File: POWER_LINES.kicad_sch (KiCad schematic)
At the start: 30 parts

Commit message: 2nd ADE
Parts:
- added H5: 0031.8201.G, 00318201G, symbol SamacSys_Parts:0031.8201.G
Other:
- note added: "Connector and fuse"
- moved on the sheet: C39, C40, C41, C42, C43, C44, C45, C46, Csns1, Csns2, R26, R27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

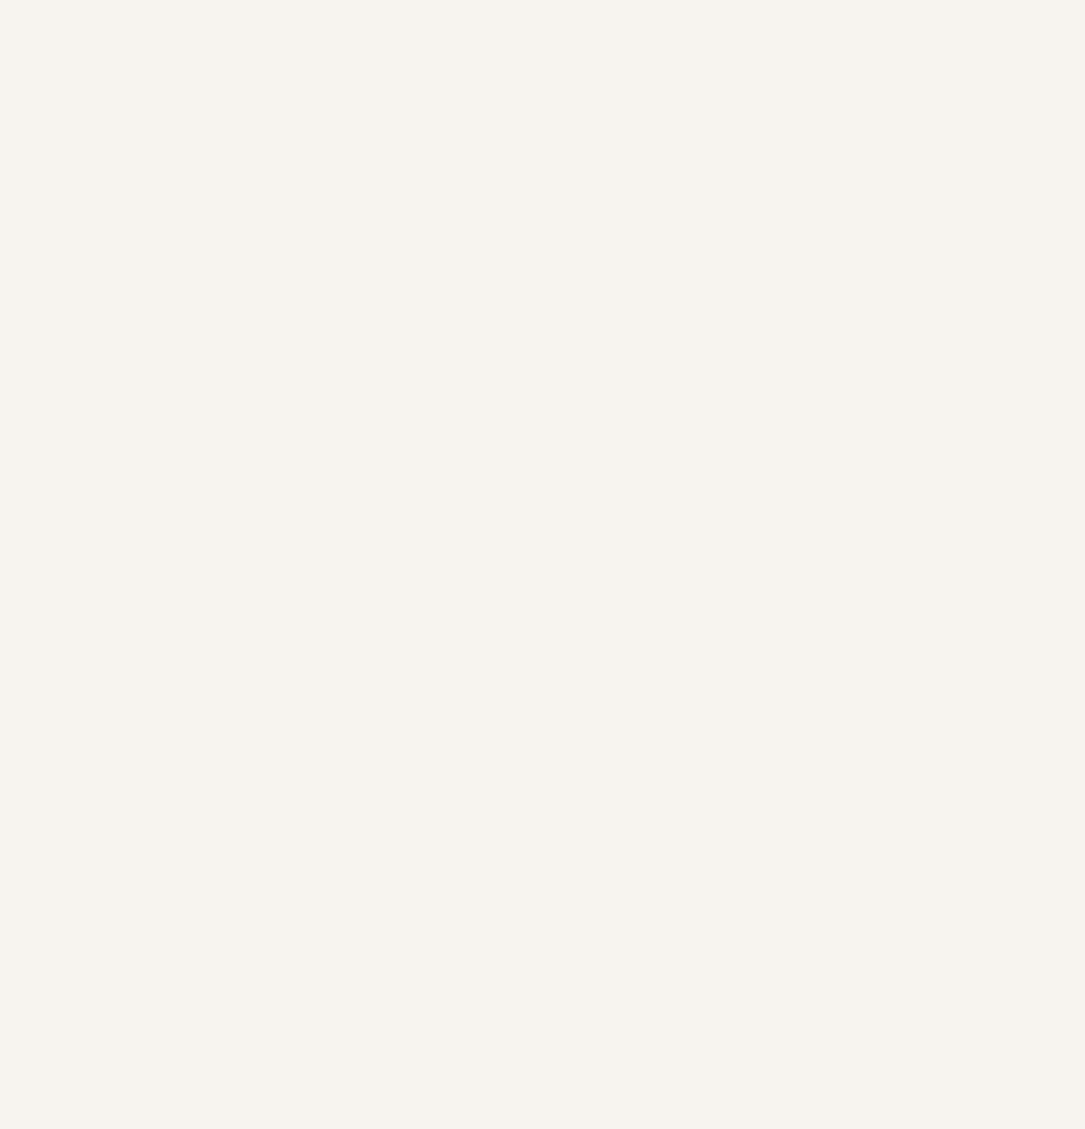
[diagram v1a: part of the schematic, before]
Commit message: ADDED RELAY
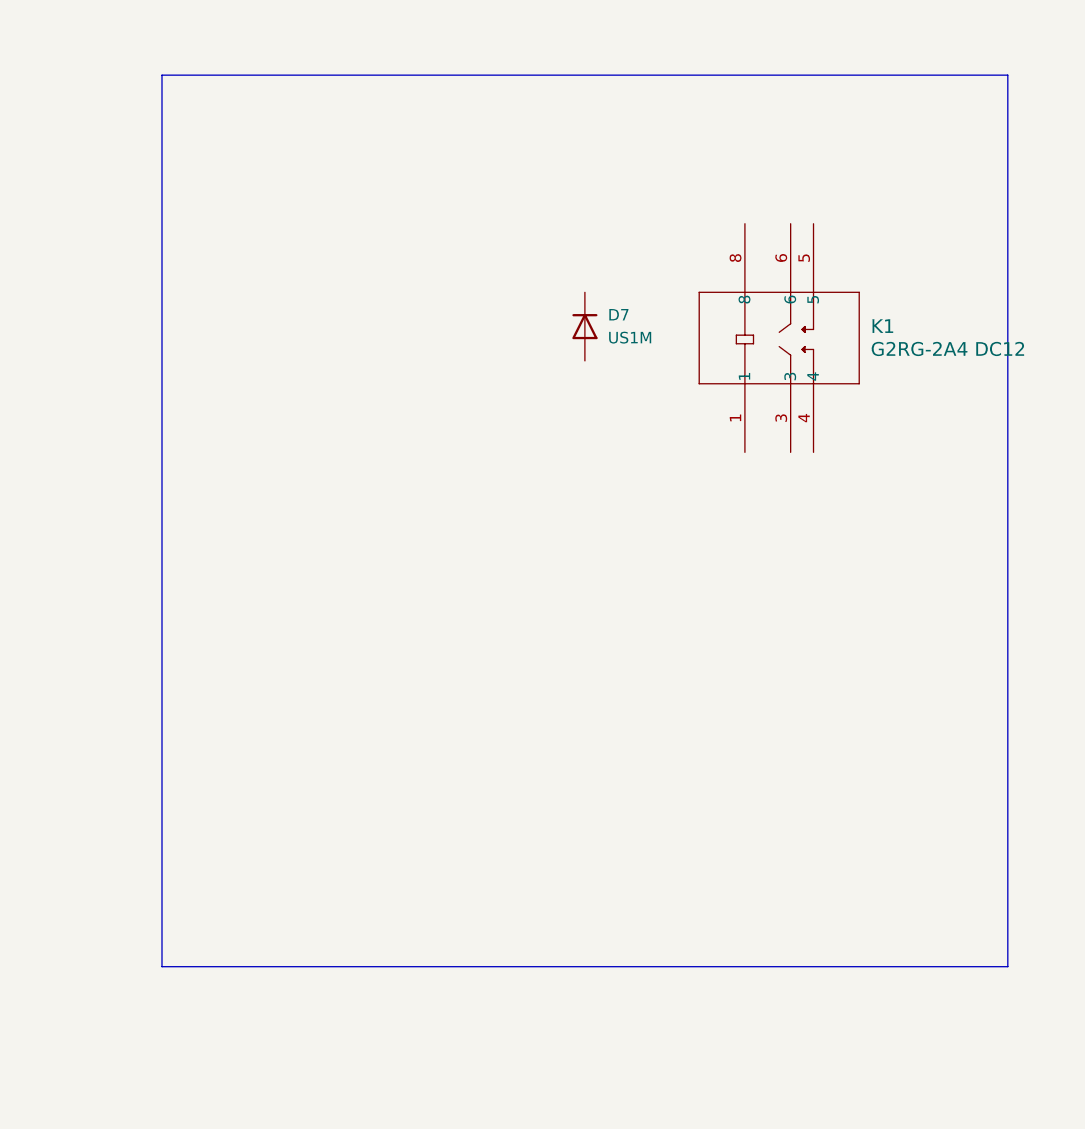
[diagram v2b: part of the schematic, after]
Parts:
- added D7: US1M, Diode_SMD:D_SMA, symbol Diode:US1M
- added K1: G2RG-2A4 DC12, RELAY_G2R-2A AC12_OMR, symbol SmartSupplyLib:G2RG-2A4_DC12
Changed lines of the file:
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@@
 	)
 	(rectangle
+		(start 175.26 20.32)
+		(end 269.24 119.38)
+		(stroke
+			(width 0)
+			(type default)
+		)
+		(fill
+			(type none)
+		)
+	)
+	(rectangle
 		(start 13.97 96.52)
 		(end 83.82 146.05)
@@
 	)
 	(symbol
+		(lib_id "SmartSupplyLib:G2RG-2A4_DC12")
+		(at 241.3 78.74 90)
+		(unit 1)
+		(body_style 1)
+		(exclude_from_sim no)
+		(in_bom yes)
+		(on_board yes)
+		(in_pos_files yes)
+		(dnp no)
+		(fields_autoplaced yes)
+		(property "Reference" "K1"
+			(at 254 48.2599 90)
+			(show_name no)
+			(do_not_autoplace no)
+			(effects
+				(font
+					(size 1.524 1.524)
+				)
+				(justify right)
+			)
+		)
+		(property "Value" "G2RG-2A4 DC12"
+			(at 254 50.7999 90)
+			(show_name no)
+			(do_not_autoplace no)
+			(effects
+				(font
+					(size 1.524 1.524)
+				)
+				(justify right)
+			)
+		)
+		(property "Footprint" "RELAY_G2R-2A AC12_OMR"
+			(at 240.03 62.23 0)
+			(hide yes)
+			(show_name no)
+			(do_not_autoplace no)
+			(effects
+				(font
+					(size 1.27 1.27)
+					(italic yes)
+				)
+			)
+		)
+		(property "Datasheet" "G2RG-2A4 DC12"
+			(at 240.03 62.23 0)
+			(hide yes)
+			(show_name no)
+			(do_not_autoplace no)
+			(effects
+				(font
+					(size 1.27 1.27)
+					(italic yes)
+				)
+			)
+		)
+		(property "Description" ""
+			(at 241.3 78.74 0)
+			(hide yes)
+			(show_name no)
+			(do_not_autoplace no)
+			(effects
+				(font
+					(size 1.27 1.27)
+				)
+			)
+		)
+		(pin "5"
+		)
+		(pin "1"
+		)
+		(pin "8"
+		)
+		(pin "3"
+		)
+		(pin "4"
+		)
+		(pin "6"
+		)
+		(instances
+			(project "smart_supply"
+				(path "/487ef637-7a03-4925-80c1-798e0c6f0bbd/34ab41b0-567d-4411-99e8-070d64ace837"
+					(reference "K1")
+					(unit 1)
+				)
+			)
+		)
+	)
+	(symbol
 		(lib_id "Device:R")
 		(at 24.13 107.95 90)
@@
 					(unit 1)
 				)
+			)
+		)
+	)
+	(symbol
+		(lib_id "Diode:US1M")
+		(at 222.25 48.26 270)
+		(unit 1)
+		(body_style 1)
+		(exclude_from_sim no)
+		(in_bom yes)
+		(on_board yes)
+		(in_pos_files yes)
+		(dnp no)
+		(fields_autoplaced yes)
+		(property "Reference" "D7"
+			(at 224.79 46.9899 90)
+			(show_name no)
+			(do_not_autoplace no)
+			(effects
+				(font
+					(size 1.27 1.27)
+				)
+				(justify left)
+			)
+		)
+		(property "Value" "US1M"
+			(at 224.79 49.5299 90)
+			(show_name no)
+			(do_not_autoplace no)
+			(effects
+				(font
+					(size 1.27 1.27)
+				)
+				(justify left)
+			)
+		)
+		(property "Footprint" "Diode_SMD:D_SMA"
+			(at 217.805 48.26 0)
+			(hide yes)
+			(show_name no)
+			(do_not_autoplace no)
+			(effects
+				(font
+					(size 1.27 1.27)
+				)
+			)
+		)
+		(property "Datasheet" "https://www.diodes.com/assets/Datasheets/ds16008.pdf"
+			(at 222.25 48.26 0)
+			(hide yes)
+			(show_name no)
+			(do_not_autoplace no)
+			(effects
+				(font
+					(size 1.27 1.27)
+				)
+			)
+		)
+		(property "Description" "1000V, 1A, General Purpose Rectifier Diode, SMA(DO-214AC)"
+			(at 222.25 48.26 0)
+			(hide yes)
+			(show_name no)
+			(do_not_autoplace no)
+			(effects
+				(font
+					(size 1.27 1.27)
+				)
+			)
+		)
+		(property "Sim.Device" "D"
+			(at 222.25 48.26 0)
+			(hide yes)
+			(show_name no)
+			(do_not_autoplace no)
+			(effects
+				(font
+					(size 1.27 1.27)
+				)
+			)
+		)
+		(property "Sim.Pins" "1=K 2=A"
+			(at 222.25 48.26 0)
+			(hide yes)
+			(show_name no)
+			(do_not_autoplace no)
+			(effects
+				(font
+					(size 1.27 1.27)
+				)
+			)
+		)
+		(pin "1"
+		)
+		(pin "2"
+		)
+		(instances
+			(project "smart_supply"
+				(path "/487ef637-7a03-4925-80c1-798e0c6f0bbd/34ab41b0-567d-4411-99e8-070d64ace837"
+					(reference "D7")
+					(unit 1)
+				)

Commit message: relay connections
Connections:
- net at K1.1: now also D7.2 (A)
- net +5V: now reaches K1.8
- net +5V: now also D7.1 (K)
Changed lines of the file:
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@@
+	)
+	(junction
+		(at 222.25 34.29)
+		(diameter 0)
+		(color 0 0 0 0)
 	)
 	(junction
@@
 	(wire
 		(pts
+			(xy 222.25 34.29) (xy 240.03 34.29)
+		)
+		(stroke
+			(width 0)
+			(type default)
+		)
+	)
+	(wire
+		(pts
 			(xy 49.53 17.78) (xy 55.88 17.78)
 		)
@@
 	(wire
 		(pts
+			(xy 222.25 52.07) (xy 222.25 64.77)
+		)
+		(stroke
+			(width 0)
+			(type default)
+		)
+	)
+	(wire
+		(pts
 			(xy 73.66 114.3) (xy 73.66 116.84)
 		)
@@
 	(wire
 		(pts
+			(xy 240.03 34.29) (xy 240.03 36.83)
+		)
+		(stroke
+			(width 0)
+			(type default)
+		)
+	)
+	(wire
+		(pts
 			(xy 52.07 184.15) (xy 52.07 187.96)
 		)
@@
 	(wire
 		(pts
+			(xy 222.25 27.94) (xy 222.25 34.29)
+		)
+		(stroke
+			(width 0)
+			(type default)
+		)
+	)
+	(wire
+		(pts
 			(xy 53.34 154.94) (xy 57.15 154.94)
 		)
@@
 	(wire
 		(pts
+			(xy 240.03 62.23) (xy 240.03 64.77)
+		)
+		(stroke
+			(width 0)
+			(type default)
+		)
+	)
+	(wire
+		(pts
 			(xy 97.79 124.46) (xy 97.79 135.89)
 		)
@@
 	(wire
 		(pts
+			(xy 222.25 34.29) (xy 222.25 44.45)
+		)
+		(stroke
+			(width 0)
+			(type default)
+		)
+	)
+	(wire
+		(pts
 			(xy 127 125.73) (xy 127 123.19)
 		)
@@
 		(pts
 			(xy 127 186.69) (xy 130.81 186.69)
+		)
+		(stroke
+			(width 0)
+			(type default)
+		)
+	)
+	(wire
+		(pts
+			(xy 222.25 64.77) (xy 240.03 64.77)
 		)
 		(stroke
@@
 					(unit 1)
 				)
+			)
+		)
+	)
+	(symbol
+		(lib_id "power:+3.3V")
+		(at 222.25 27.94 0)
+		(unit 1)
+		(body_style 1)
+		(exclude_from_sim no)
+		(in_bom yes)
+		(on_board yes)
+		(in_pos_files yes)
+		(dnp no)
+		(fields_autoplaced yes)
+		(property "Reference" "#PWR033"
+			(at 222.25 31.75 0)
+			(hide yes)
+			(show_name no)
+			(do_not_autoplace no)
+			(effects
+				(font
+					(size 1.27 1.27)
+				)
+			)
+		)
+		(property "Value" "+5V"
+			(at 222.25 22.86 0)
+			(show_name no)
+			(do_not_autoplace no)
+			(effects
+				(font
+					(size 1.27 1.27)
+				)
+			)
+		)
+		(property "Footprint" "Package_DFN_QFN:Diodes_UDFN3810-9_TYPE_B"
+			(at 222.25 27.94 0)
+			(hide yes)
+			(show_name no)
+			(do_not_autoplace no)
+			(effects
+				(font
+					(size 1.27 1.27)
+				)
+			)
+		)
+		(property "Datasheet" ""
+			(at 222.25 27.94 0)
+			(hide yes)
+			(show_name no)
+			(do_not_autoplace no)
+			(effects
+				(font
+					(size 1.27 1.27)
+				)
+			)
+		)
+		(property "Description" "Power symbol creates a global label with name \"+3.3V\""
+			(at 222.25 27.94 0)
+			(hide yes)
+			(show_name no)
+			(do_not_autoplace no)
+			(effects
+				(font
+					(size 1.27 1.27)
+				)
+			)
+		)
+		(pin "1"
+		)
+		(instances
+			(project "smart_supply"
+				(path "/487ef637-7a03-4925-80c1-798e0c6f0bbd/34ab41b0-567d-4411-99e8-070d64ace837"
+					(reference "#PWR033")
+					(unit 1)
+				)

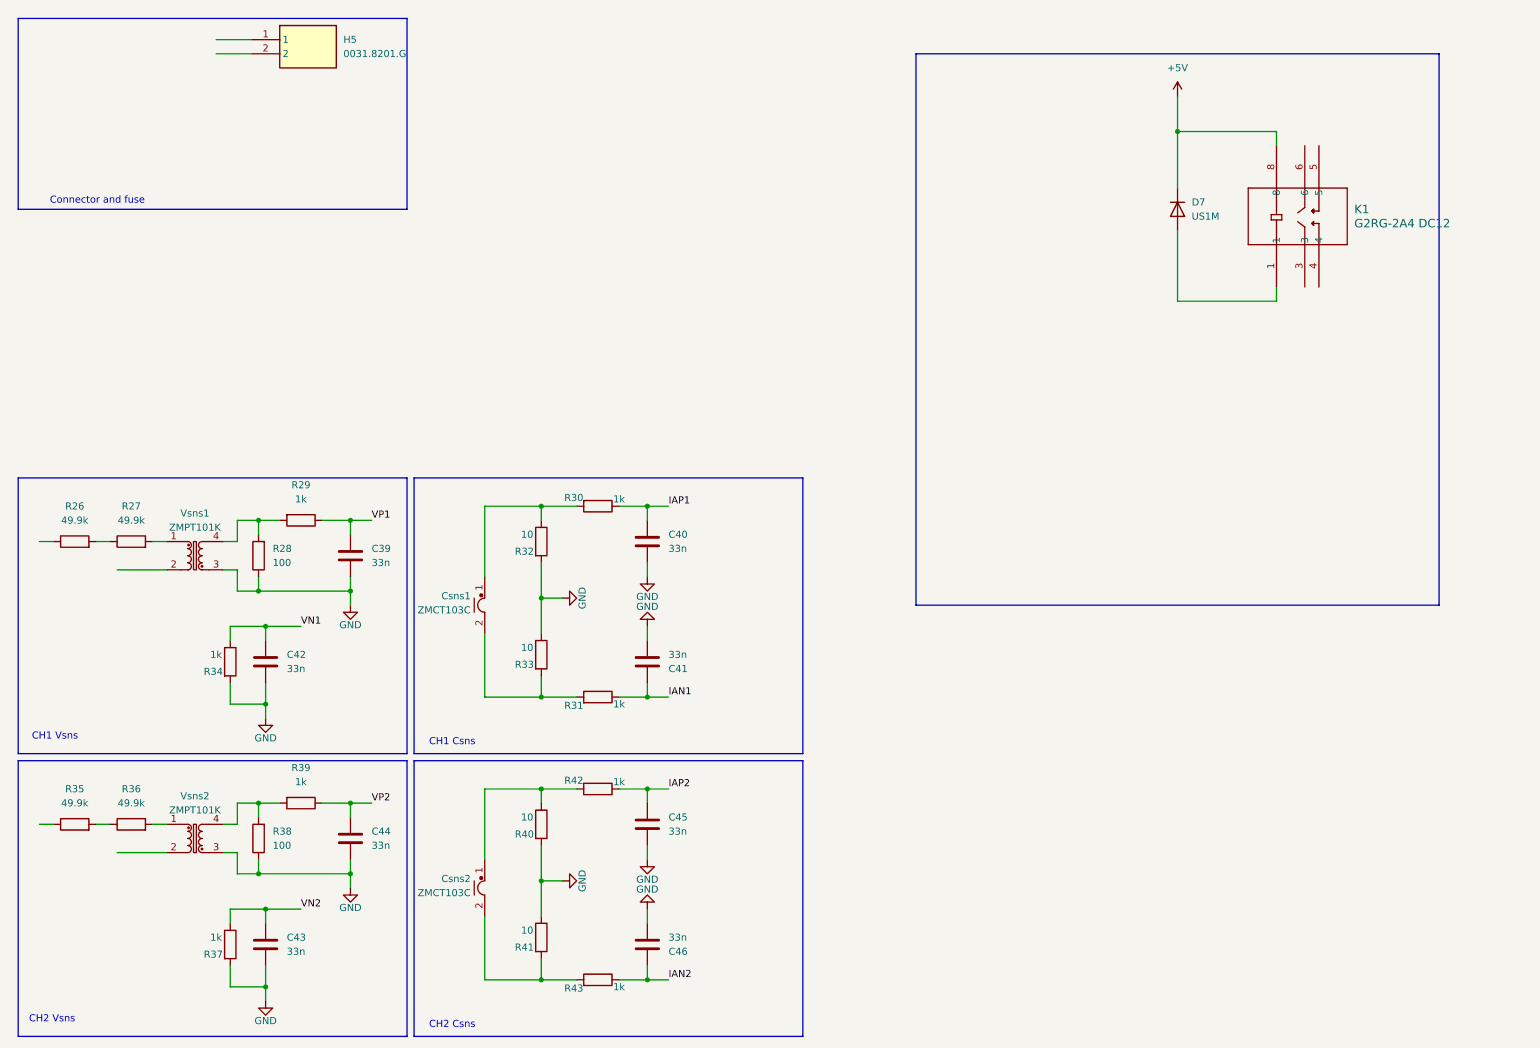
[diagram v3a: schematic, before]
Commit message: POWER LINE SHEET DRAFT FINISHED
Added CH2 transformer, fuses and connectors. Foorprints TBD. Relay modules finished and assigned to MCU. VSNS and CSNS connected to lines.
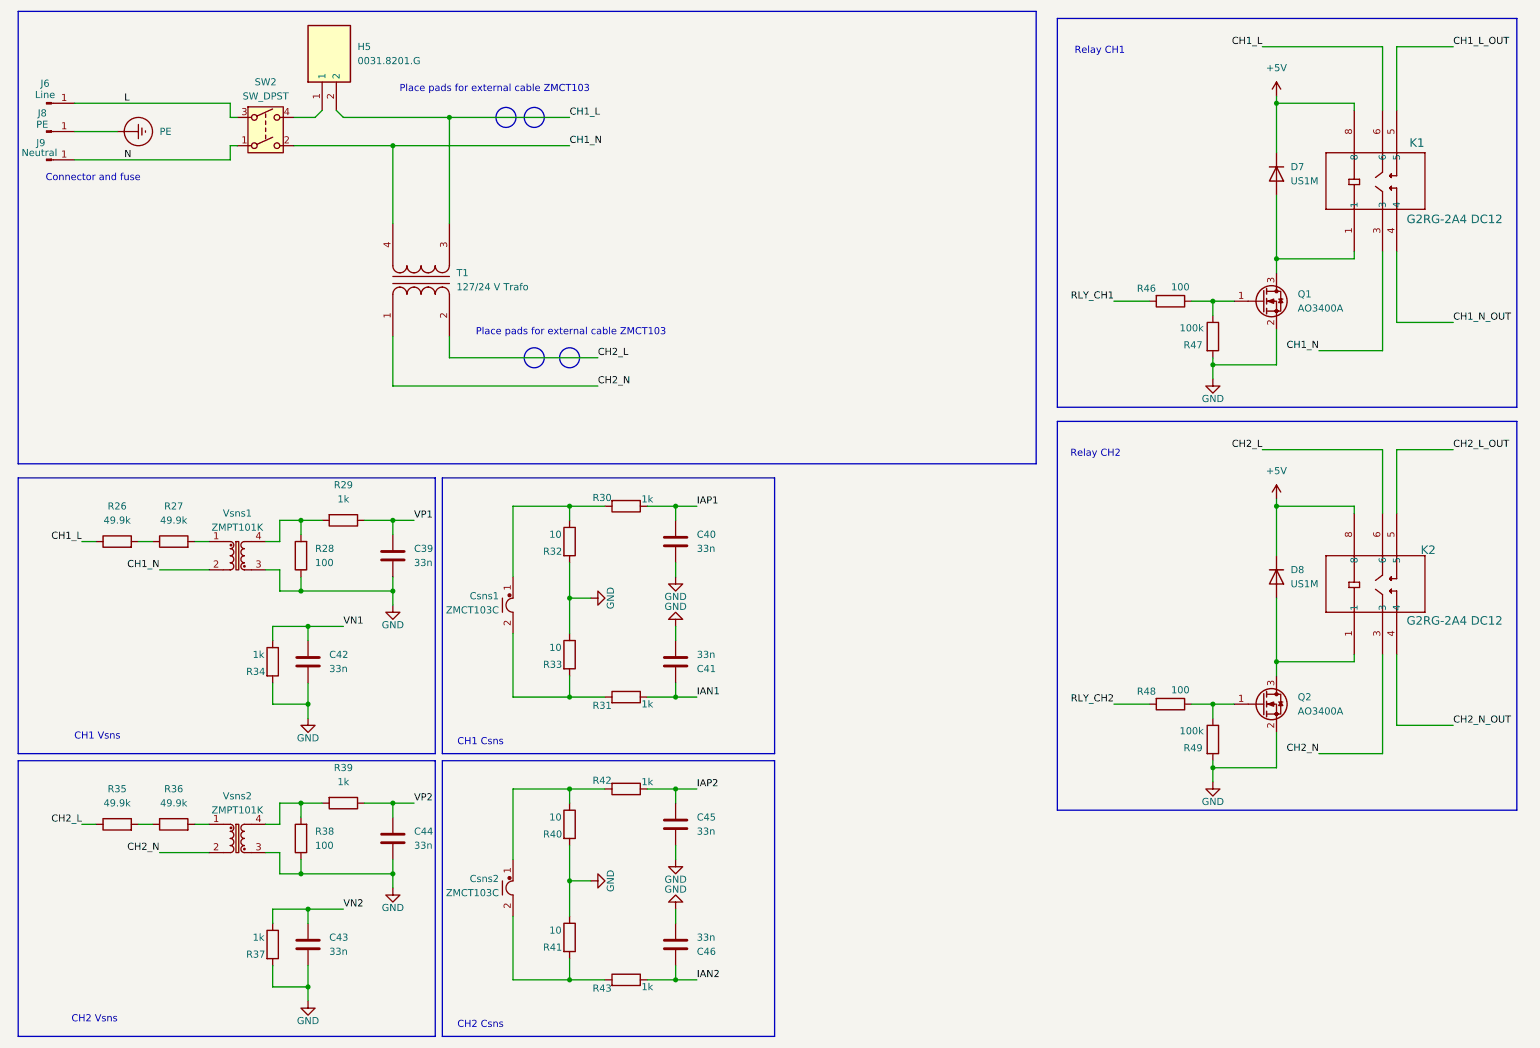
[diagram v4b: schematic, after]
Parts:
- added D8: US1M, Diode_SMD:D_SMA, symbol Diode:US1M
- added J6: Line, Connector:Tag-Connect_TC2030-IDC-FP_2x03_P1.27mm_Vertical, symbol Connector:Conn_01x01_Pin
- added J8: PE, Connector:Tag-Connect_TC2030-IDC-FP_2x03_P1.27mm_Vertical, symbol Connector:Conn_01x01_Pin
- added J9: Neutral, Connector:Tag-Connect_TC2030-IDC-FP_2x03_P1.27mm_Vertical, symbol Connector:Conn_01x01_Pin
- added K2: G2RG-2A4 DC12, RELAY_G2R-2A AC12_OMR, symbol SmartSupplyLib:G2RG-2A4_DC12
- added Q1, Q2: AO3400A, Package_TO_SOT_SMD:SOT-23, symbol Transistor_FET:AO3400A
- added R46, R48: 100, Package_DIP:DIP-8_W7.62mm, symbol Device:R
- added R47, R49: 100k, Package_DIP:DIP-8_W7.62mm, symbol Device:R
- added SW2: SW_DPST, Button_Switch_THT:SW_NKK_GW12LJP, symbol Switch:SW_DPST
- added T1: 127/24 V Trafo, symbol Device:Transformer_1P_1S
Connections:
- net +5V: now also D8.1 (K), K2.8
- net GND: now also Q1.2 (S), Q2.2 (S), R47.2, R49.2
- net CH2_L: now reaches R35.1
- net CH2_L: now also K2.6, T1.2 (AB)
- net CH1_N: now reaches Vsns1.2
- net CH1_N: now also K1.3, SW2.2, T1.4 (SB)
- net CH2_N: now reaches Vsns2.2
- net CH2_N: now also K2.3, T1.1 (AA)
- net at D7.2 (A), K1.1: now also Q1.3 (D)
- net CH1_N_OUT: now reaches K1.4
- net CH1_L_OUT: now reaches K1.5
- net CH1_L: now reaches K1.6
- net CH1_L: now also H5.2, R26.1, T1.3 (SA)
- net at H5.1: now also SW2.4
- new net: Q1.1 (G), R46.1, R47.1
- new net: Q2.1 (G), R48.1, R49.1
- new net: D8.2 (A), K2.1, Q2.3 (D)
- new net CH2_L_OUT: K2.5
- new net CH2_N_OUT: K2.4
- new net L: J6.1 (Pin_1), SW2.3
- new net N: J9.1 (Pin_1), SW2.1
- new net PE: J8.1 (Pin_1)
- new net RLY_CH1: R46.2
- new net RLY_CH2: R48.2
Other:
- note added: "Place pads for external cable ZMCT103"
- note added: "Relay CH1"
- note added: "Relay CH2"
- moved on the sheet: C39, C40, C41, C42, C43, C44, C45, C46, Csns1, Csns2, D7, K1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

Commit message: CHANGED RELAYS AND CONNECTORS
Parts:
- removed D7, D8: US1M, Diode_SMD:D_SMA, symbol Diode:US1M
- removed J6: Line, Connector:Tag-Connect_TC2030-IDC-FP_2x03_P1.27mm_Vertical, symbol Connector:Conn_01x01_Pin
- removed J8: PE, Connector:Tag-Connect_TC2030-IDC-FP_2x03_P1.27mm_Vertical, symbol Connector:Conn_01x01_Pin
- removed J9: Neutral, Connector:Tag-Connect_TC2030-IDC-FP_2x03_P1.27mm_Vertical, symbol Connector:Conn_01x01_Pin
- removed K1, K2: G2RG-2A4 DC12, RELAY_G2R-2A AC12_OMR, symbol SmartSupplyLib:G2RG-2A4_DC12
- removed Q1, Q2: AO3400A, Package_TO_SOT_SMD:SOT-23, symbol Transistor_FET:AO3400A
- removed R35: 49.9k, Package_DIP:DIP-8_W7.62mm, symbol Device:R
- removed R46, R48: 100, Package_DIP:DIP-8_W7.62mm, symbol Device:R
- removed R47, R49: 100k, Package_DIP:DIP-8_W7.62mm, symbol Device:R
- removed T1: 127/24 V Trafo, symbol Device:Transformer_1P_1S
- added D10, D7, D8, D9: 1N4007, Diode_THT:D_DO-41_SOD81_P10.16mm_Horizontal, symbol Diode:1N4007
- added J6: 1730405, CONN_1730405_PXC, symbol SmartSupplyLib:1730405
- added J8, J9: 1717020, CONN_1717020_PXC, symbol SmartSupplyLib:1717020
- added K3, K4, K5, K6: G2R-1A-E DC5, RELAY_G2R-1A-E AC12_OMR, symbol SmartSupplyLib:G2R-1A-E_DC6
- added Q3, Q4: AO3400A, Package_TO_SOT_SMD:SOT-23, symbol Transistor_FET:AO3400A
- added R50, R52: 100, Package_DIP:DIP-8_W7.62mm, symbol Device:R
- added R51, R53: 100k, Package_DIP:DIP-8_W7.62mm, symbol Device:R
- R36: value 49.9k -> 20k
- R40, R41: value 10 -> 33
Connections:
- net +5V: now also D10.1 (K), D7.1 (K), D8.1 (K), D9.1 (K), K3.8, K4.8, K5.8, K6.8
- net CH1_L: now also J8.1, K4.3, K4.6
- net CH1_L_OUT: now also K4.4, K4.5
- net CH1_N: now also J8.2, K3.3, K3.6
- net CH1_N_OUT: now also K3.4, K3.5
- net CH2_L: now also R36.1, J9.2, K5.3, K5.6
- net CH2_L_OUT: now also K5.4, K5.5
- net CH2_N: now also J9.1, K6.3, K6.6
- net CH2_N_OUT: now also K6.4, K6.5
- net GND: now also Q3.2 (S), Q4.2 (S), R51.2, R53.2
- net L: now also J6.1
- net N: now also J6.3
- net PE: now also J6.2
- net RLY_CH1: now also R50.2
- net RLY_CH2: now also R52.2
- new net: D10.2 (A), D8.2 (A), K5.1, K6.1, Q4.3 (D)
- new net: D7.2 (A), D9.2 (A), K3.1, K4.1, Q3.3 (D)
- new net: Q4.1 (G), R52.1, R53.1
- new net: Q3.1 (G), R50.1, R51.1
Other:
- note added: "Relay CH1 L"
- note added: "Relay CH1 N"
- note removed: "Relay CH1"
- note removed: "Relay CH2"
- moved on the sheet: R36
